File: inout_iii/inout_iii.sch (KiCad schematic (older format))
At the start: 1 part, among them P1 DIN_41612_128P

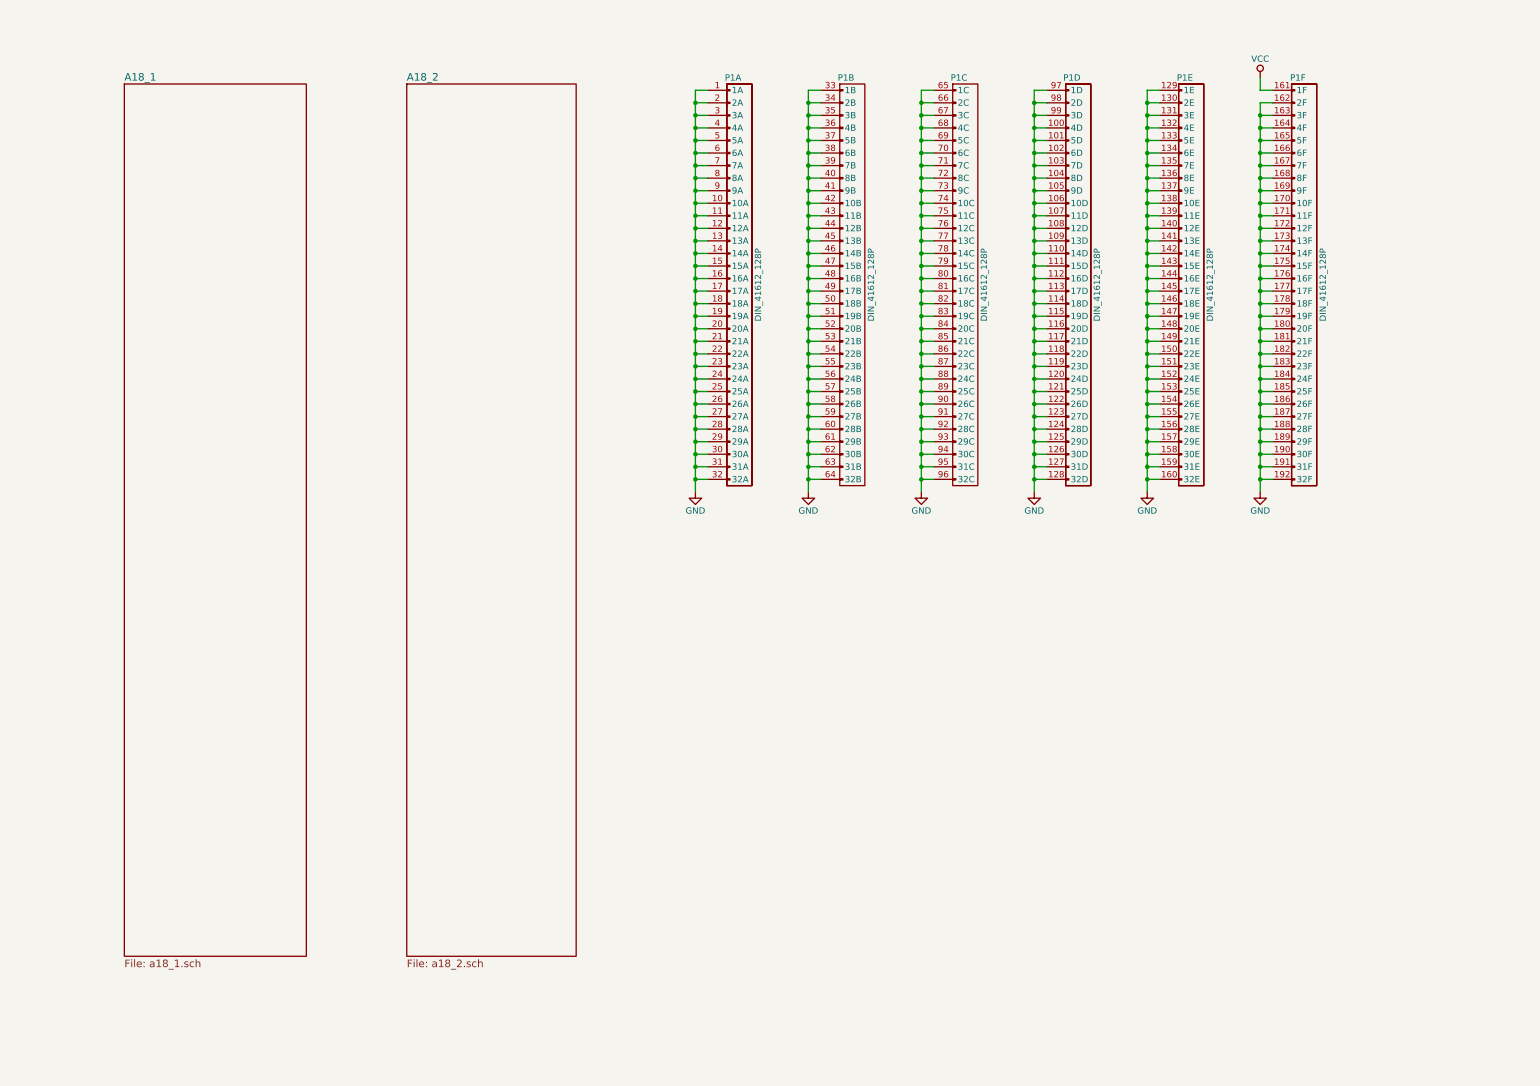
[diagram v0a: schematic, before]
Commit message: Added most of the rest of Inout III and tied it in. Still not sure where to put the downlink stuff, standby, and CHOR propers.
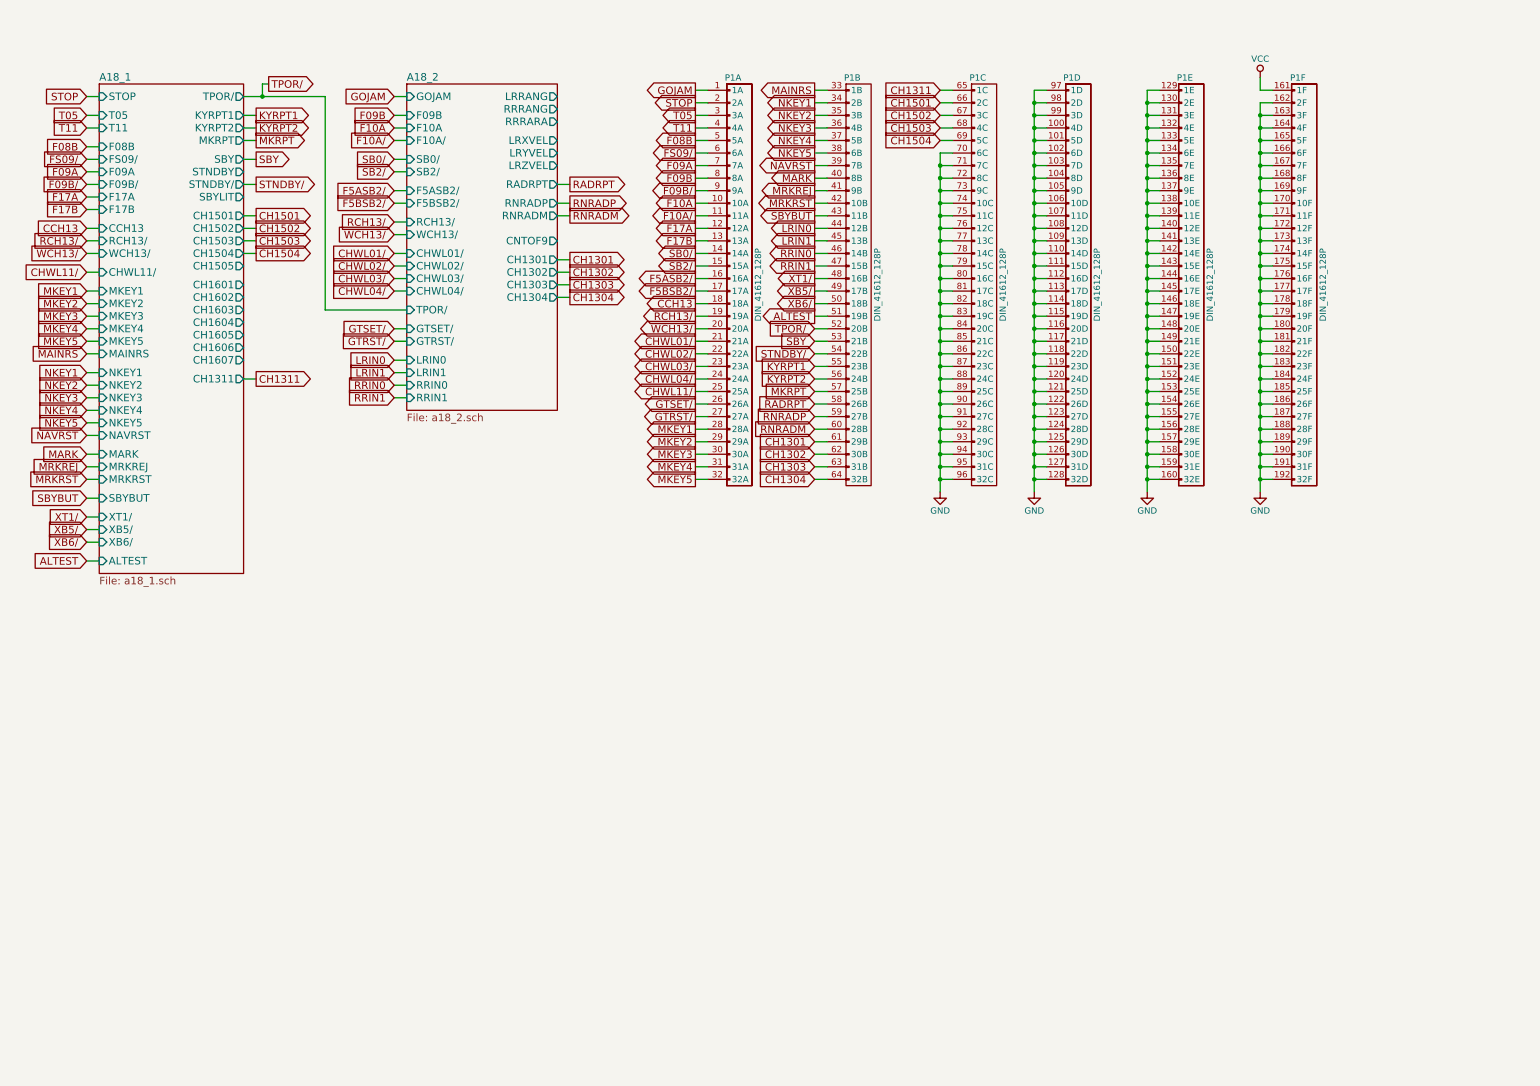
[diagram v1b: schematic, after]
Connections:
- net GND: no longer P1.1 (1A), P1.10 (10A), P1.11 (11A), P1.12 (12A), P1.13 (13A), P1.14 (14A), P1.15 (15A), P1.16 (16A), P1.17 (17A), P1.18 (18A), P1.19 (19A), P1.2 (2A), P1.20 (20A), P1.21 (21A), P1.22 (22A), P1.23 (23A), P1.24 (24A), P1.25 (25A), P1.26 (26A), P1.27 (27A), P1.28 (28A), P1.29 (29A), P1.3 (3A), P1.30 (30A), P1.31 (31A), P1.32 (32A), P1.33 (1B), P1.34 (2B), P1.35 (3B), P1.36 (4B), P1.37 (5B), P1.38 (6B), P1.39 (7B), P1.4 (4A), P1.40 (8B), P1.41 (9B), P1.42 (10B), P1.43 (11B), P1.44 (12B), P1.45 (13B), P1.46 (14B), P1.47 (15B), P1.48 (16B), P1.49 (17B), P1.5 (5A), P1.50 (18B), P1.51 (19B), P1.52 (20B), P1.53 (21B), P1.54 (22B), P1.55 (23B), P1.56 (24B), P1.57 (25B), P1.58 (26B), P1.59 (27B), P1.6 (6A), P1.60 (28B), P1.61 (29B), P1.62 (30B), P1.63 (31B), P1.64 (32B), P1.65 (1C), P1.66 (2C), P1.67 (3C), P1.68 (4C), P1.69 (5C), P1.7 (7A), P1.8 (8A), P1.9 (9A)
- new net ALTEST: P1.51 (19B)
- new net CCH13: P1.18 (18A)
- new net CH1301: P1.61 (29B)
- new net CH1302: P1.62 (30B)
- new net CH1303: P1.63 (31B)
- new net CH1304: P1.64 (32B)
- new net CH1311: P1.65 (1C)
- new net CH1501: P1.66 (2C)
- new net CH1502: P1.67 (3C)
- new net CH1503: P1.68 (4C)
- new net CH1504: P1.69 (5C)
- new net CHWL01/: P1.21 (21A)
- new net CHWL02/: P1.22 (22A)
- new net CHWL03/: P1.23 (23A)
- new net CHWL04/: P1.24 (24A)
- new net CHWL11/: P1.25 (25A)
- new net F08B: P1.5 (5A)
- new net F09A: P1.7 (7A)
- new net F09B: P1.8 (8A)
- new net F09B/: P1.9 (9A)
- new net F10A: P1.10 (10A)
- new net F10A/: P1.11 (11A)
- new net F17A: P1.12 (12A)
- new net F17B: P1.13 (13A)
- new net F5ASB2/: P1.16 (16A)
- new net F5BSB2/: P1.17 (17A)
- new net FS09/: P1.6 (6A)
- new net GOJAM: P1.1 (1A)
- new net GTRST/: P1.27 (27A)
- new net GTSET/: P1.26 (26A)
- new net KYRPT1: P1.55 (23B)
- new net KYRPT2: P1.56 (24B)
- new net LRIN0: P1.44 (12B)
- new net LRIN1: P1.45 (13B)
- new net MAINRS: P1.33 (1B)
- new net MARK: P1.40 (8B)
- new net MKEY1: P1.28 (28A)
- new net MKEY2: P1.29 (29A)
- new net MKEY3: P1.30 (30A)
- new net MKEY4: P1.31 (31A)
- new net MKEY5: P1.32 (32A)
- new net MKRPT: P1.57 (25B)
- new net MRKREJ: P1.41 (9B)
- new net MRKRST: P1.42 (10B)
- new net NAVRST: P1.39 (7B)
- new net NKEY1: P1.34 (2B)
- new net NKEY2: P1.35 (3B)
- new net NKEY3: P1.36 (4B)
- new net NKEY4: P1.37 (5B)
- new net NKEY5: P1.38 (6B)
- new net RADRPT: P1.58 (26B)
- new net RCH13/: P1.19 (19A)
- new net RNRADM: P1.60 (28B)
- new net RNRADP: P1.59 (27B)
- new net RRIN0: P1.46 (14B)
- new net RRIN1: P1.47 (15B)
- new net SB0/: P1.14 (14A)
- new net SB2/: P1.15 (15A)
- new net SBY: P1.53 (21B)
- new net SBYBUT: P1.43 (11B)
- new net STNDBY/: P1.54 (22B)
- new net STOP: P1.2 (2A)
- new net T05: P1.3 (3A)
- new net T11: P1.4 (4A)
- new net TPOR/: P1.52 (20B)
- new net WCH13/: P1.20 (20A)
- new net XB5/: P1.49 (17B)
- new net XB6/: P1.50 (18B)
- new net XT1/: P1.48 (16B)
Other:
- moved on the sheet: P1B, P1C

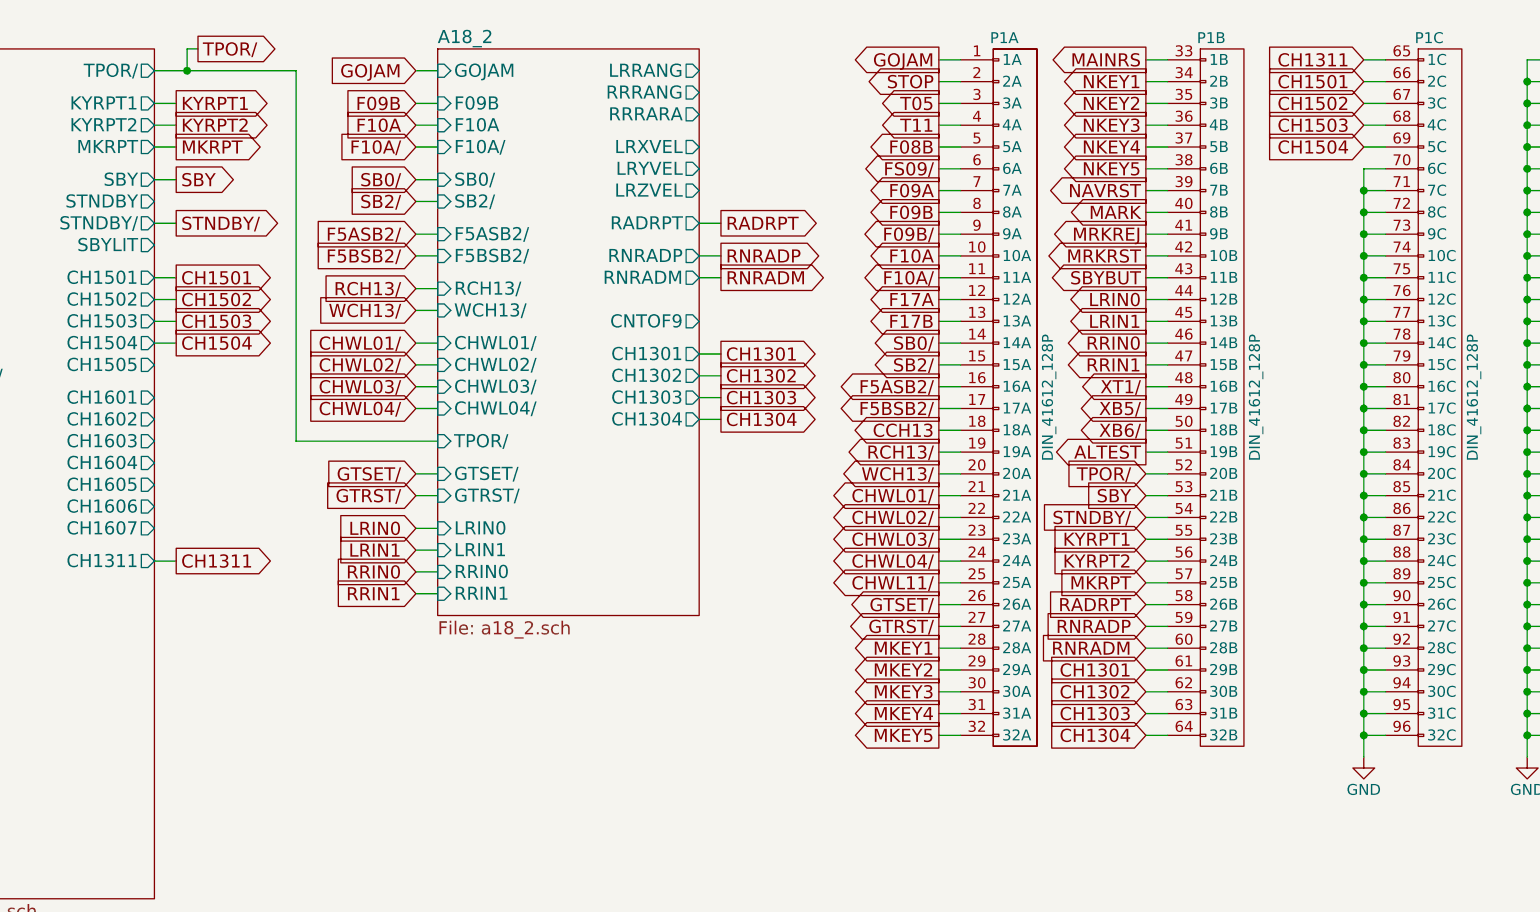
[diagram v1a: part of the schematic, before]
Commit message: Added and tied in Inout VII, the final logic module!
I still need to comb through the schematics to see if there are any
stray gates I missed. The initial conditions are also pretty much
guaranteed to be wrong. But it's mostly all there!
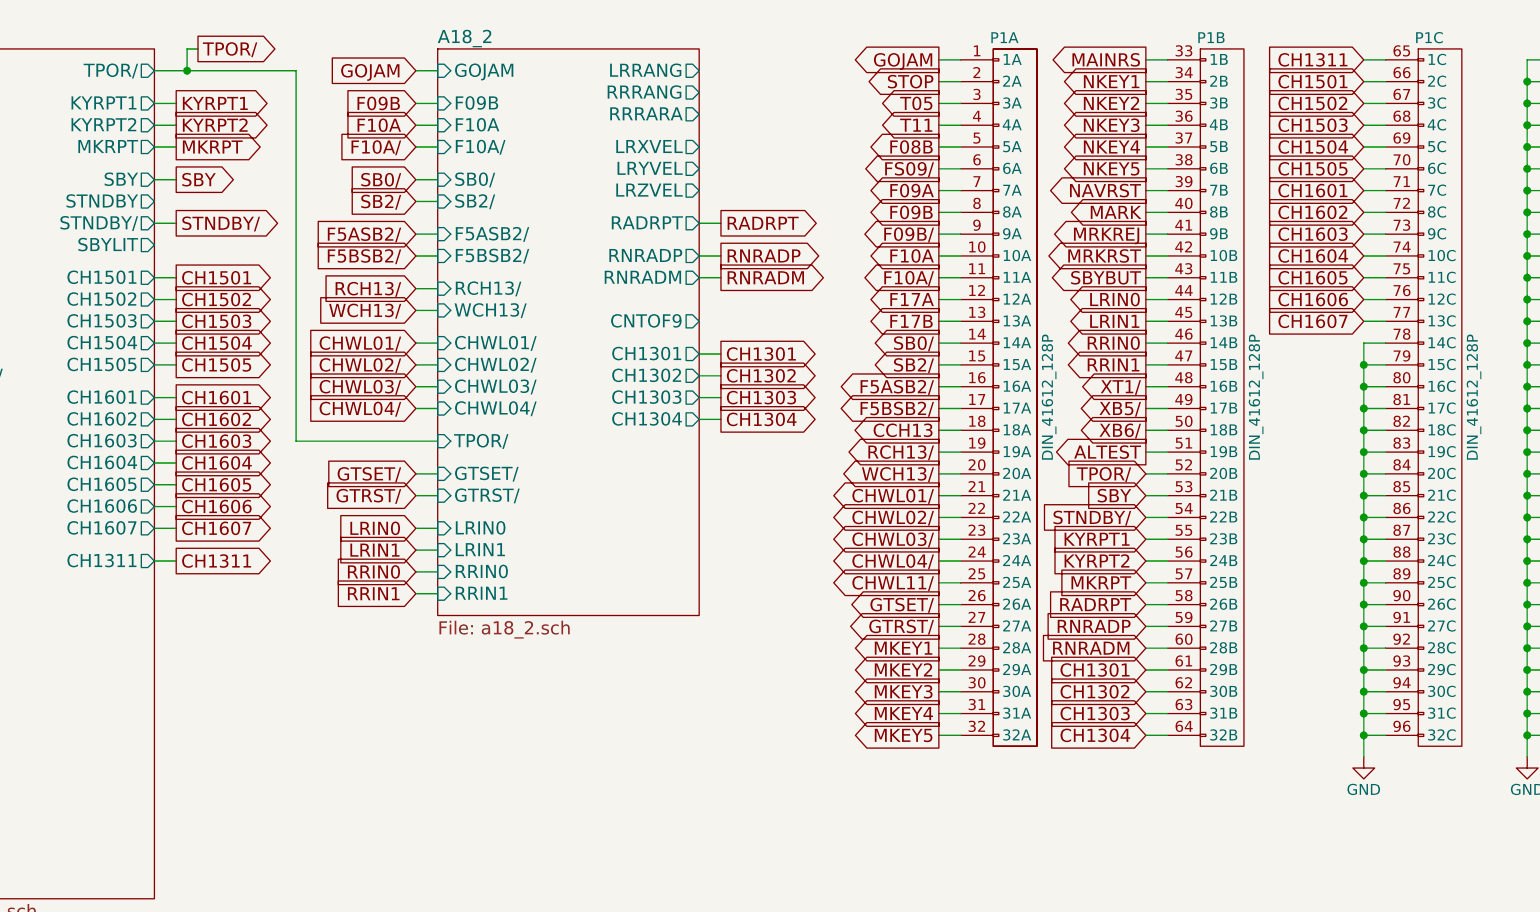
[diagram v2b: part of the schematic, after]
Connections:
- net GND: no longer P1.70 (6C), P1.71 (7C), P1.72 (8C), P1.73 (9C), P1.74 (10C), P1.75 (11C), P1.76 (12C), P1.77 (13C)
- new net CH1505: P1.70 (6C)
- new net CH1601: P1.71 (7C)
- new net CH1602: P1.72 (8C)
- new net CH1603: P1.73 (9C)
- new net CH1604: P1.74 (10C)
- new net CH1605: P1.75 (11C)
- new net CH1606: P1.76 (12C)
- new net CH1607: P1.77 (13C)
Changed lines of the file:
@@
 $EndComp
 Wire Wire Line
-	8350 1850 8450 1850
-Wire Wire Line
-	8350 1950 8450 1950
-Connection ~ 8350 1950
-Wire Wire Line
-	8350 2050 8450 2050
-Connection ~ 8350 2050
-Wire Wire Line
-	8350 2150 8450 2150
-Connection ~ 8350 2150
-Wire Wire Line
-	8350 2250 8450 2250
-Connection ~ 8350 2250
-Wire Wire Line
-	8350 2350 8450 2350
-Connection ~ 8350 2350
-Wire Wire Line
-	8350 2450 8450 2450
-Connection ~ 8350 2450
-Wire Wire Line
-	8350 2550 8450 2550
-Connection ~ 8350 2550
-Wire Wire Line
 	8350 2650 8450 2650
-Connection ~ 8350 2650
 Wire Wire Line
 	8350 2750 8450 2750
@@
 Connection ~ 2950 1400
 Wire Wire Line
-	8350 1850 8350 4550
-Wire Wire Line
 	7450 3250 7350 3250
 Text GLabel 7350 3250 0    60   Input ~ 0
 TPOR/
+Wire Wire Line
+	2800 2750 2900 2750
+Text GLabel 2900 2750 2    60   Output ~ 0
+CH1505
+Wire Wire Line
+	8450 1850 8350 1850
+Text GLabel 8350 1850 0    60   Input ~ 0
+CH1505
+Wire Wire Line
+	2800 2900 2900 2900
+Text GLabel 2900 2900 2    60   Output ~ 0
+CH1601
+Wire Wire Line
+	2800 3000 2900 3000
+Text GLabel 2900 3000 2    60   Output ~ 0
+CH1602
+Wire Wire Line
+	2800 3100 2900 3100
+Text GLabel 2900 3100 2    60   Output ~ 0
+CH1603
+Wire Wire Line
+	2800 3200 2900 3200
+Text GLabel 2900 3200 2    60   Output ~ 0
+CH1604
+Wire Wire Line
+	2800 3300 2900 3300
+Text GLabel 2900 3300 2    60   Output ~ 0
+CH1605
+Wire Wire Line
+	2800 3400 2900 3400
+Text GLabel 2900 3400 2    60   Output ~ 0
+CH1606
+Wire Wire Line
+	2800 3500 2900 3500
+Text GLabel 2900 3500 2    60   Output ~ 0
+CH1607
+Wire Wire Line
+	8450 1950 8350 1950
+Text GLabel 8350 1950 0    60   Input ~ 0
+CH1601
+Wire Wire Line
+	8450 2050 8350 2050
+Text GLabel 8350 2050 0    60   Input ~ 0
+CH1602
+Wire Wire Line
+	8450 2150 8350 2150
+Text GLabel 8350 2150 0    60   Input ~ 0
+CH1603
+Wire Wire Line
+	8450 2250 8350 2250
+Text GLabel 8350 2250 0    60   Input ~ 0
+CH1604
+Wire Wire Line
+	8450 2350 8350 2350
+Text GLabel 8350 2350 0    60   Input ~ 0
+CH1605
+Wire Wire Line
+	8450 2450 8350 2450
+Text GLabel 8350 2450 0    60   Input ~ 0
+CH1606
+Wire Wire Line
+	8450 2550 8350 2550
+Text GLabel 8350 2550 0    60   Input ~ 0
+CH1607
+Wire Wire Line
+	8350 2650 8350 4550
 $EndSCHEMATC

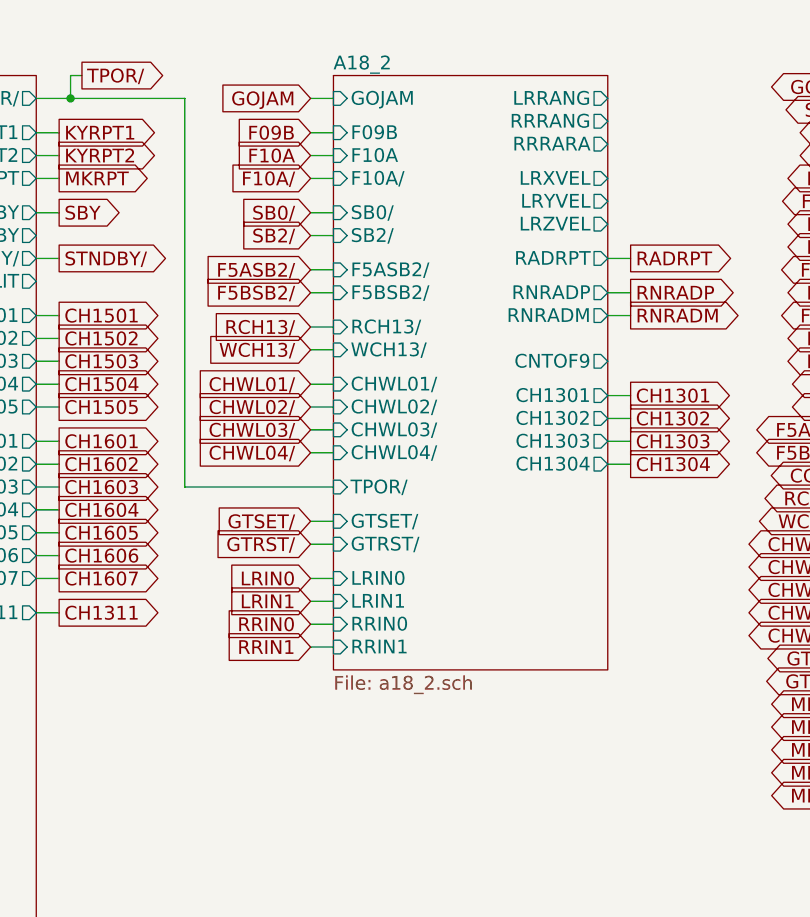
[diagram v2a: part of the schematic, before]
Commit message: Lots of initial conditions, some missed gates, and some wiring fixes
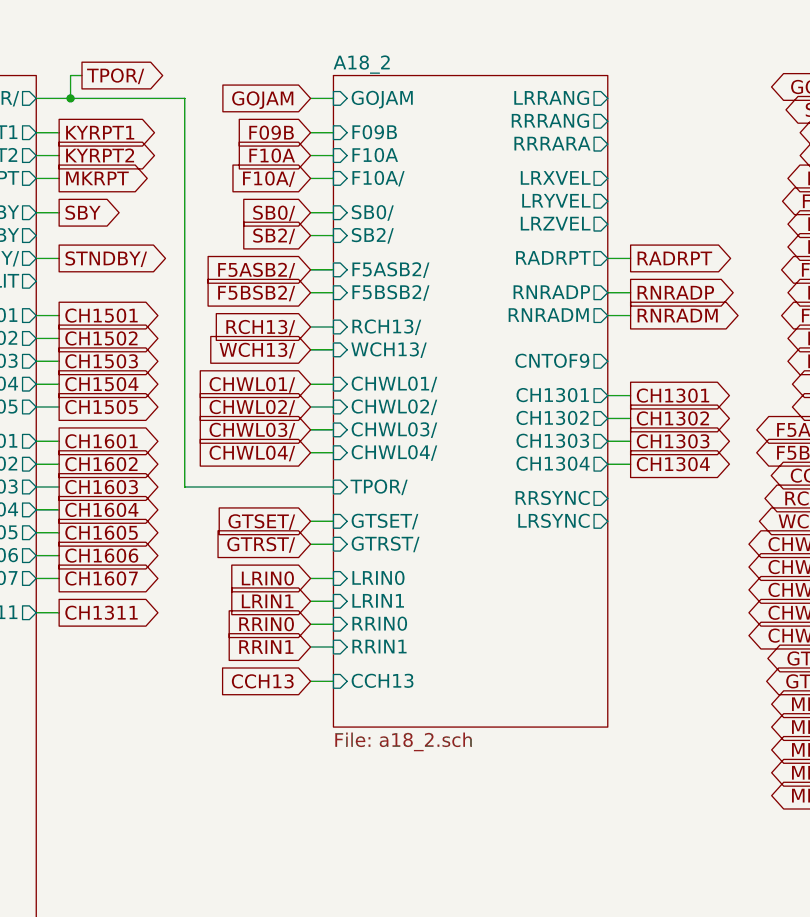
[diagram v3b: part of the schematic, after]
